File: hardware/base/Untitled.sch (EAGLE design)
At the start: 36 parts, among them Q1 IRLML2502, Q2 IRLML2502, Q3 IRLML2502, Q4 IRLML2502, U1 ATMEGA328P, U2 MIC5205, Y1 16MHZ

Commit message: new commit.
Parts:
- removed C7, C8: 0.1uF, SparkFun-Capacitors:CAP0402-CAP
- removed LED1: Green, SparkFun-LED:LED0603
- removed R2: 10K, SparkFun-Passives:RESISTOR0402-RES
- removed R3: 330, SparkFun-Passives:RESISTOR0402-RES
- removed U1: ATMEGA328P, SparkFun-DigitalIC:ATMEGA328_SMT
- removed Y1: 16MHZ, SparkFun-FreqCtrl:RESONATOR16MHZ
- added R1: 1K, SparkFun-Passives:RESISTOR0402-RES
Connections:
- removed net AREF: C7.2, U1.AREF
- removed net CE: U1.PB0(ICP)
- removed net CSN: U1.PD7(AIN1)
- removed net D10: R13.1, R14.2, U1.PB2(SS/OC1B)
- removed net D5: R7.1, R8.1, U1.PD5(T1)
- removed net D6: R10.2, R9.1, U1.PD6(AIN0)
- removed net D9: R11.1, R12.2, U1.PB1(OC1A)
- removed net MISO: U1.PB4(MISO)
- removed net MOSI: U1.PB3(MOSI/OC2)
- removed net N$10: U1.PB6(XTAL1/TOSC1), Y1.1
- removed net N$15: U$2.TX
- removed net N$16: U$2.CH_PD
- removed net N$17: U$2.GPIO14
- removed net N$18: U$2.GPIO12
- removed net N$19: LED1.A, R3.1
- removed net N$20: U$2.GPIO13
- removed net N$22: U$2.GND
- removed net N$6: U$2.RX
- removed net N$9: U1.PB7(XTAL2/TOSC2), Y1.3
- removed net RESET: C8.1, R2.1, U1.PC6(/RESET)
- removed net RXI: FTDI.TXO, U1.PD0(RXD)
- removed net SCK: R3.2, U1.PB5(SCK)
- removed net TXO: FTDI.RXI, U1.PD1(TXD)
- new net M1: R7.1, R8.1, U$2.GPIO14
- new net M2: R10.2, R9.1, U$2.GPIO12
- new net M3: R11.1, R12.2, U$2.GPIO13
- new net M4: R13.1, R14.2, U$2.GPIO16
- new net RX: FTDI.TXO, U$2.RX
- new net TX: FTDI.RXI, U$2.TX
- net 3.3V: now also U$2.CH_PD, U$2.GPIO2
- net 5V: no longer FTDI.VCC, R2.2, U1.AVCC, U1.VCC@1, U1.VCC@2
- net DTR: now also U$2.GPIO0; no longer C8.2
- net GND: now also R1.1, U$2.GND; no longer C7.1, LED1.C, U1.AGND, U1.GND@1, U1.GND@2, Y1.2
- net N$21: now also R1.2
- net SCL: no longer U1.PC5(ADC5/SCL)
- net SDA: no longer U1.PC4(ADC4/SDA)
- net VCC: now also FTDI.VCC
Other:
- note added: "主控"
- note added: "传感器"
- note added: "发动机"
- note added: "电源"
- note removed: "Motor"
- note removed: "Power"
- moved on the sheet: C1, C10, C14, C2, C6, C9, JP3, JP4, JP5, JP6, POWER, Q1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

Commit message: 20160415
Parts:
- removed C9: 0.1uF, SparkFun-Capacitors:CAP0402-CAP
- removed U$2: ESP07, esp8266modules:ESP07
- added U$3: ESP12, esp8266modules:ESP12
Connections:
- removed net 5V: C9.1
- removed net N$21: R1.2, U$2.GPIO15
- new net N$20: R1.2, U$3.GPIO15
- net 3.3V: now also U$3.CH_PD, U$3.GPIO2, U$3.VCC; no longer U$2.CH_PD, U$2.GPIO2, U$2.VCC
- net DTR: now also U$3.GPIO0; no longer U$2.GPIO0
- net GND: now also U$3.GND; no longer C9.2, U$2.GND
- net M1: now also U$3.GPIO14; no longer U$2.GPIO14
- net M2: now also U$3.GPIO12; no longer U$2.GPIO12
- net M3: now also U$3.GPIO13; no longer U$2.GPIO13
- net M4: now also U$3.GPIO16; no longer U$2.GPIO16
- net RX: now also U$3.RX; no longer U$2.RX
- net SCL: now also U$3.GPIO4
- net SDA: now also U$3.GPIO5
- net TX: now also U$3.TX; no longer U$2.TX
- net VCC: now also U$3.ADC
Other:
- moved on the sheet: R1

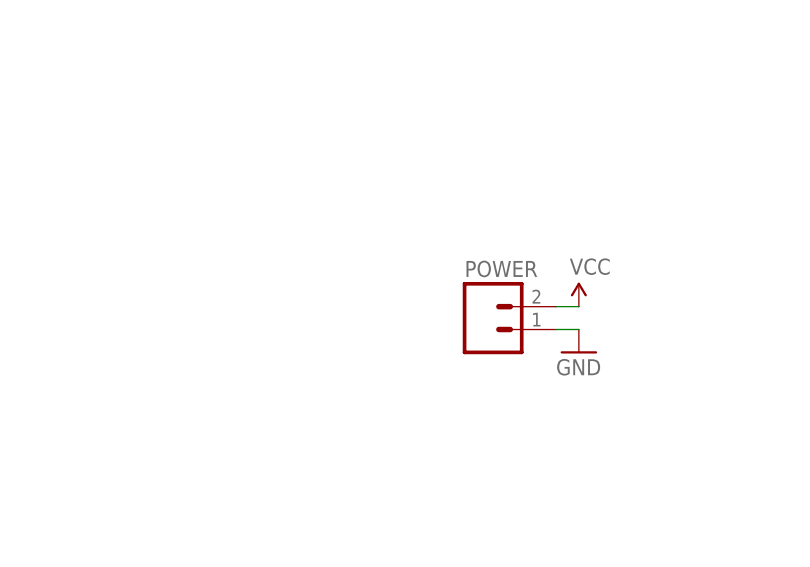
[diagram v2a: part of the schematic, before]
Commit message: add switch
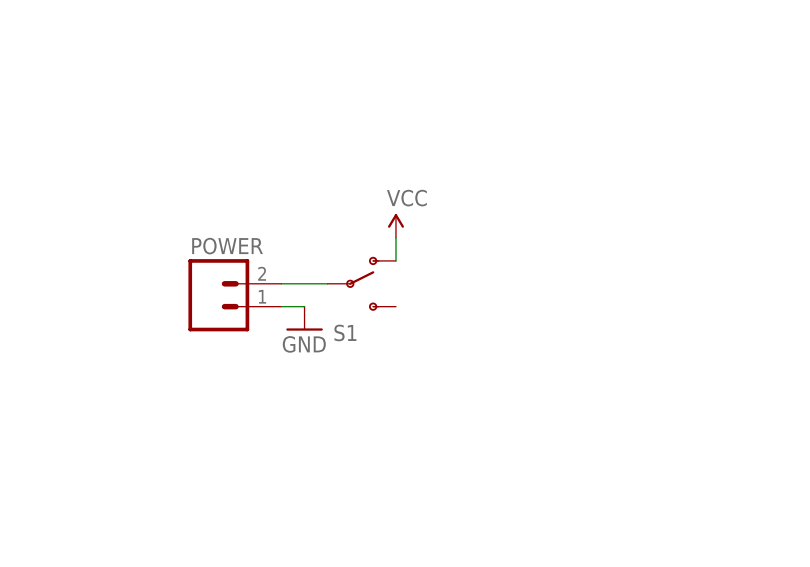
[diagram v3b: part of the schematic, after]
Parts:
- added S1: (no value), SparkFun-Electromechanical:SWITCH-SPDTSMD2
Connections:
- new net N$6: POWER.2, S1.P
- net VCC: now also S1.O; no longer POWER.2
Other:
- moved on the sheet: POWER
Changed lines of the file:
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@@
 <part name="U$3" library="esp8266modules" deviceset="ESP12" device=""/>
 <part name="GND1" library="SparkFun-Aesthetics" deviceset="GND" device=""/>
+<part name="S1" library="SparkFun-Electromechanical" deviceset="SWITCH-SPDT" device="SMD2"/>
 </parts>
 <sheets>
@@
 <instance part="R13" gate="G$1" x="96.52" y="-50.8"/>
 <instance part="R14" gate="G$1" x="86.36" y="-55.88" rot="R90"/>
-<instance part="POWER" gate="G$1" x="12.7" y="15.24"/>
-<instance part="GND6" gate="1" x="22.86" y="12.7"/>
+<instance part="POWER" gate="G$1" x="-17.78" y="17.78"/>
+<instance part="GND6" gate="1" x="-7.62" y="15.24"/>
 <instance part="JP3" gate="G$1" x="116.84" y="-35.56" rot="R180"/>
 <instance part="JP4" gate="G$1" x="116.84" y="10.16" rot="R180"/>
@@
 <instance part="SUPPLY7" gate="G$1" x="-48.26" y="-38.1"/>
 <instance part="SUPPLY8" gate="G$1" x="-5.08" y="-38.1"/>
-<instance part="SUPPLY10" gate="G$1" x="22.86" y="17.78"/>
+<instance part="SUPPLY10" gate="G$1" x="2.54" y="25.4"/>
 <instance part="SUPPLY2" gate="G$1" x="-129.54" y="25.4" rot="R90"/>
 <instance part="R1" gate="G$1" x="-66.04" y="63.5" rot="R90"/>
@@
 <instance part="U$3" gate="G$1" x="-96.52" y="76.2"/>
 <instance part="GND1" gate="1" x="-73.66" y="63.5"/>
+<instance part="S1" gate="1" x="-2.54" y="20.32"/>
 </instances>
 <busses>
@@
 <pinref part="POWER" gate="G$1" pin="1"/>
 <pinref part="GND6" gate="1" pin="GND"/>
-<wire x1="20.32" y1="15.24" x2="22.86" y2="15.24" width="0.1524" layer="91"/>
+<wire x1="-10.16" y1="17.78" x2="-7.62" y2="17.78" width="0.1524" layer="91"/>
 </segment>
 <segment>
@@
 </net>
 <net name="VCC" class="0">
-<segment>
-<pinref part="POWER" gate="G$1" pin="2"/>
-<wire x1="20.32" y1="17.78" x2="22.86" y2="17.78" width="0.1524" layer="91"/>
-<pinref part="SUPPLY10" gate="G$1" pin="VCC"/>
-</segment>
 <segment>
 <pinref part="U2" gate="G$1" pin="IN"/>
@@
 <wire x1="-114.3" y1="81.28" x2="-121.92" y2="81.28" width="0.1524" layer="91"/>
 <label x="-121.92" y="81.28" size="1.27" layer="95" rot="R180" xref="yes"/>
+</segment>
+<segment>
+<pinref part="SUPPLY10" gate="G$1" pin="VCC"/>
+<pinref part="S1" gate="1" pin="O"/>
+<wire x1="2.54" y1="25.4" x2="2.54" y2="22.86" width="0.1524" layer="91"/>
 </segment>
 </net>
@@
 </segment>
 </net>
+<net name="N$6" class="0">
+<segment>
+<pinref part="S1" gate="1" pin="P"/>
+<pinref part="POWER" gate="G$1" pin="2"/>
+<wire x1="-5.08" y1="20.32" x2="-10.16" y2="20.32" width="0.1524" layer="91"/>
+</segment>
+</net>
